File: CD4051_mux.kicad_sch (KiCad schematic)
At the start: 24 parts, among them J22 mux, U4 74HC4051M/TR

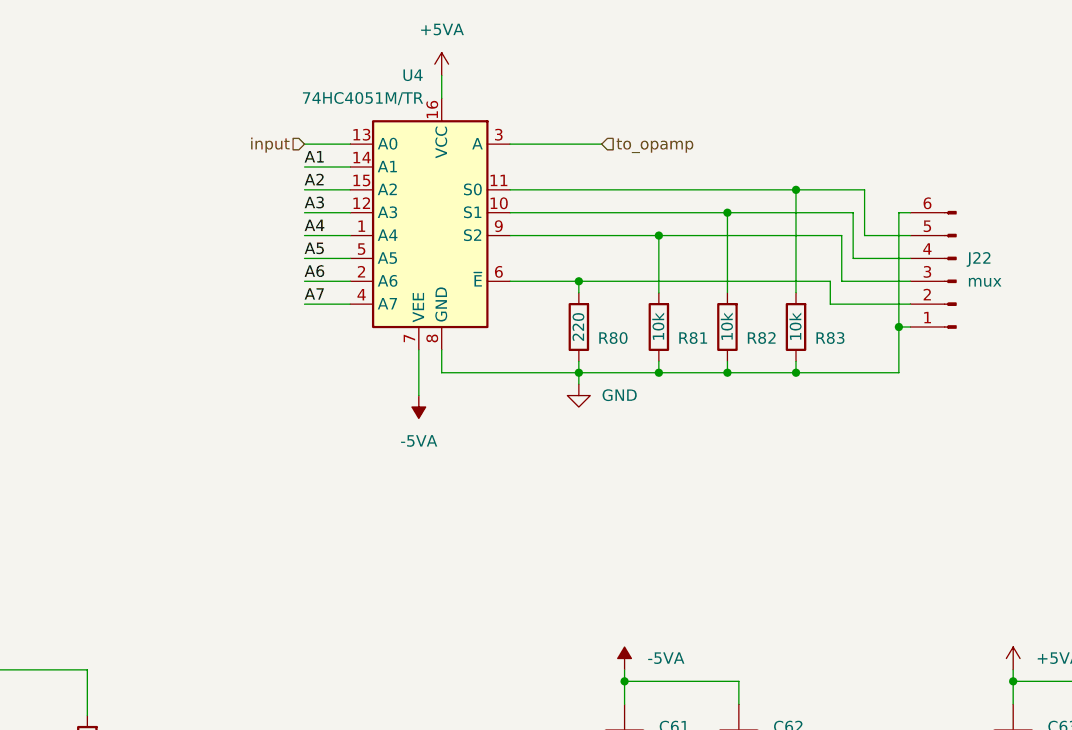
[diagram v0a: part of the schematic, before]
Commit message: Version 1.0 submitted to JLCPCB
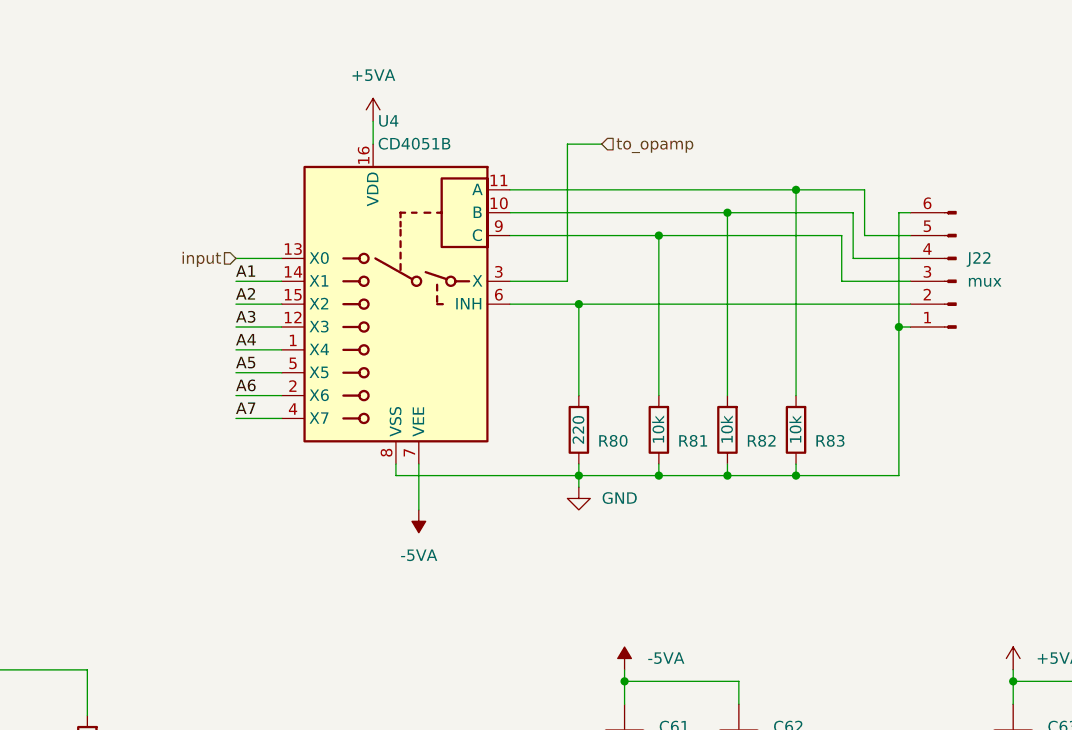
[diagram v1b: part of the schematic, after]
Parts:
- removed U4: 74HC4051M/TR, Package_SO:SOIC-16_3.9x9.9mm_P1.27mm, symbol 74xx:74HC4051
- added U4: CD4051B, Package_SO:SOIC-16_3.9x9.9mm_P1.27mm, symbol Analog_Switch:CD4051B
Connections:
- net +5VA: now also U4.16 (VDD)
- net -5VA: now also U4.7 (VEE)
- net A1: now also U4.14 (X1)
- net A2: now also U4.15 (X2)
- net A3: now also U4.12 (X3)
- net A4: now also U4.1 (X4)
- net A5: now also U4.5 (X5)
- net A6: now also U4.2 (X6)
- net A7: now also U4.4 (X7)
- net GND: now also U4.8 (VSS)
- net input: now also U4.13 (X0)
- net to_opamp: now also U4.3 (X)
- net at J22.2 (Pin_2), R80.2: now also U4.6 (INH)
- net at J22.3 (Pin_3), R81.2: now also U4.9 (C)
- net at J22.4 (Pin_4), R82.2: now also U4.10 (B)
- net at J22.5 (Pin_5), R83.2: now also U4.11 (A)
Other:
- moved on the sheet: R80, R81, R82, R83
